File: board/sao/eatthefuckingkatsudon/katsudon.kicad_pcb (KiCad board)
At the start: 2 copper layers, 48.9 x 49.8 mm, 4 parts

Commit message: work on punching popuko sao
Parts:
- removed the G*** at (90.6, 73.6) (x4)
- added G*** (x4): LOGO, LOGO, F.Cu at (50.3, 41.6)
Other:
- board size 48.9 x 49.8 mm -> 48.2 x 48.9 mm

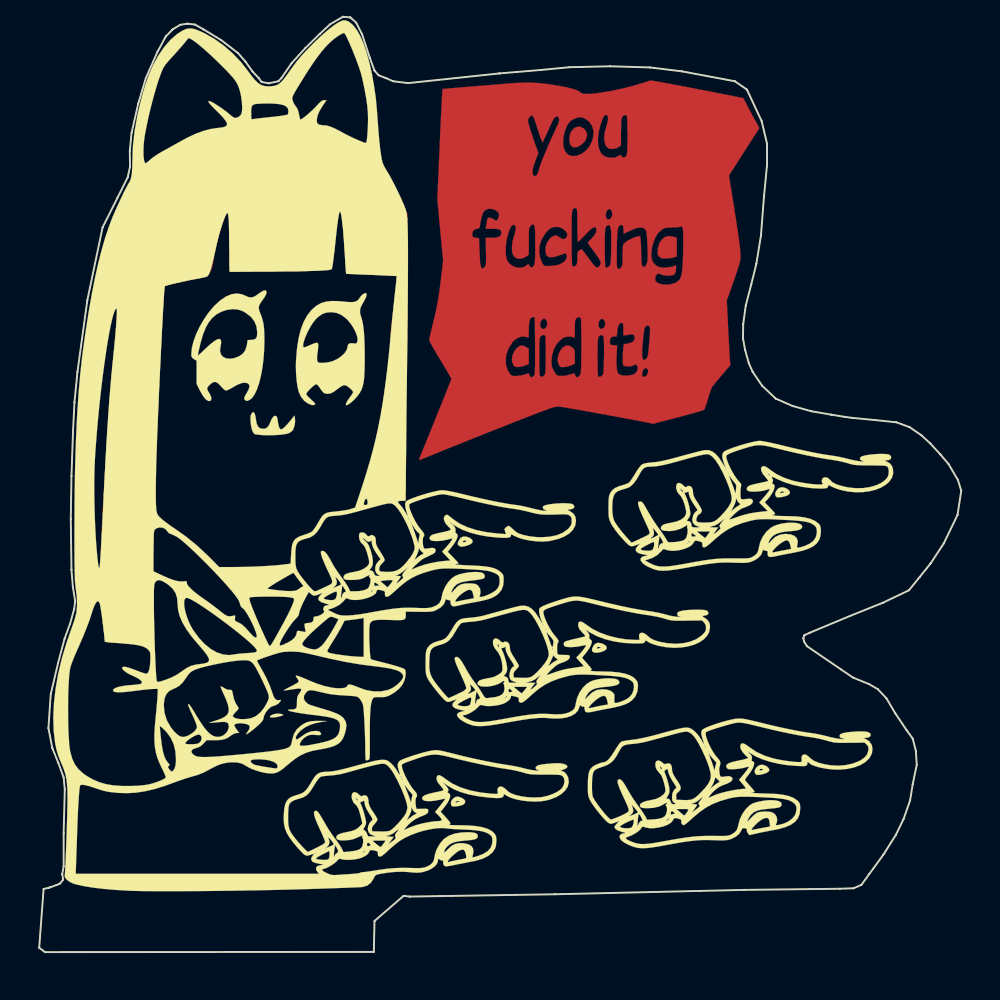
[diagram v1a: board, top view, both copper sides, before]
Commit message: wired power and LED matrix
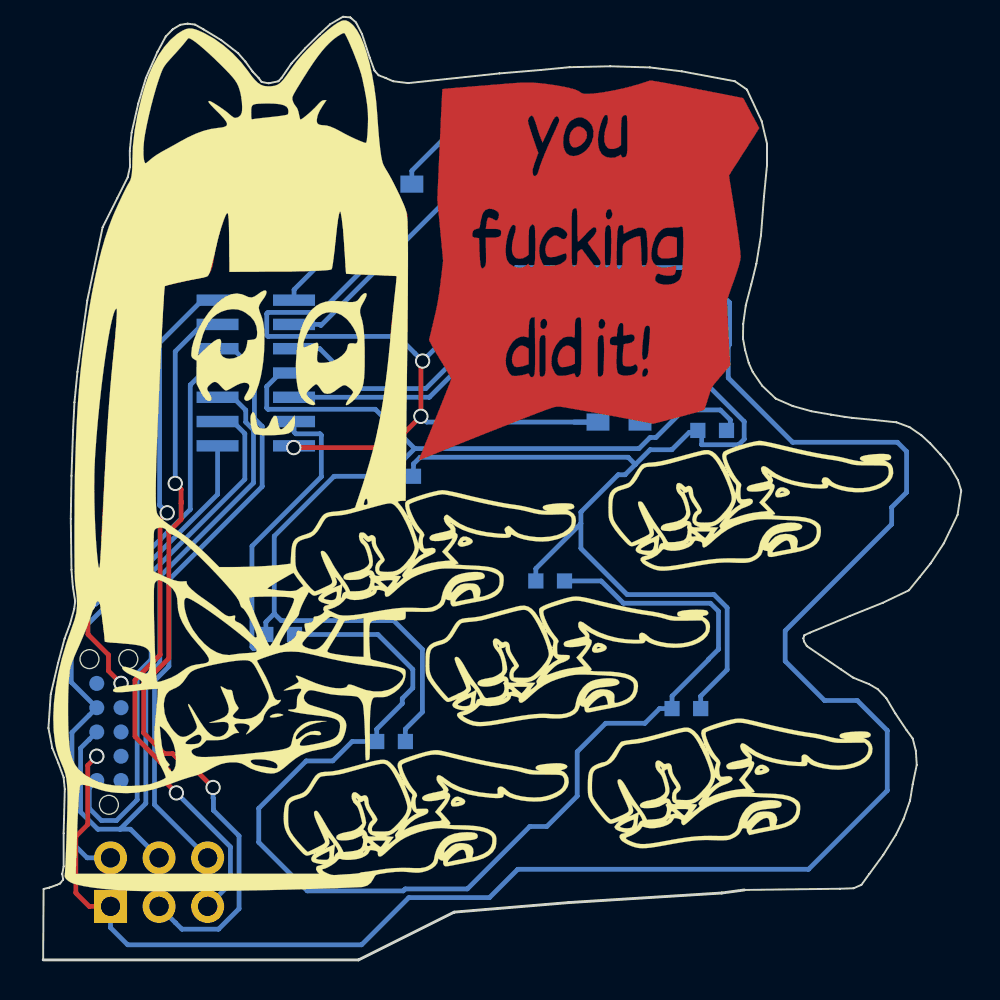
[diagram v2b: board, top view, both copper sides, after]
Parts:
- removed the G*** at (50.3, 41.6) (x4)
- added D1: LED, LEDs:LED_0603, B.Cu at (59.1, 53.9)
- added D2: LED, LEDs:LED_0603, B.Cu at (52.0, 47.2)
- added D3: LED, LEDs:LED_0603, B.Cu at (43.7, 55.6)
- added D4: LED, LEDs:LED_0603, B.Cu at (37.9, 50.0)
- added D5: LED, LEDs:LED_0603, B.Cu at (60.5, 39.3)
- added D6: LED, LEDs:LED_0603, B.Cu at (44.1, 41.7)
- added D7: LED, LEDs:LED_0603, B.Cu at (37.2, 24.4)
- added D8: LED, LEDs:LED_0603, B.Cu at (47.8, 23.9)
- added D9: LED, LEDs:LED_0603, B.Cu at (59.7, 34.8)
- added G*** (x4): LOGO, LOGO, F.Cu at (50.3, 41.6)
- added G***: LOGO, katsudon:GRANTSIG10X10, B.Cu at (45.2, 32.7)
- added IC1: ATTINY20-X, katsudon:ATTINY20_SOIC-14, B.Cu at (36.6, 36.3)
- added J1: PROG, katsudon:TC2050-All_Holes, B.Cu at (28.9, 55.1)
- added P1: SAO_PLUG, Socket_Strips:Socket_Strip_Straight_2x03, B.Cu at (29.0, 64.2)
- added R1: R, Resistors_SMD:R_0603_HandSoldering, B.Cu at (37.3, 26.5)
- added R2: R, Resistors_SMD:R_0603_HandSoldering, B.Cu at (43.7, 26.4)
- added R3: R, Resistors_SMD:R_0603_HandSoldering, B.Cu at (55.6, 38.9)
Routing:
- net GND: track 0.00 -> 171.0 mm, vias 0 -> 4
- net Net-(D1-Pad2): track 0.00 -> 81.3 mm
- net Net-(D1-Pad1): track 0.00 -> 74.1 mm
- net Net-(D3-Pad1): track 0.00 -> 58.0 mm
- net /SCL: track 0.00 -> 40.7 mm, vias 0 -> 2
- net /GPIO2: track 0.00 -> 36.9 mm, vias 0 -> 2
- net /SDA/TPIDATA: track 0.00 -> 36.4 mm
- net /GPIO1: track 0.00 -> 31.6 mm
- net /TPICLK: track 0.00 -> 28.0 mm
- net +3V3: track 0.00 -> 27.4 mm
- net Net-(D9-Pad2): track 0.00 -> 25.2 mm
- net /RESET: track 0.00 -> 20.5 mm, vias 0 -> 2
- net Net-(D8-Pad2): track 0.00 -> 13.8 mm
- net Net-(D7-Pad2): track 0.00 -> 9.96 mm
- net Net-(D8-Pad1): track 0.00 -> 5.18 mm
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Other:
- board size 48.2 x 48.9 mm -> 48 x 49.3 mm
- net class Default: clearance 0.2 -> 0.2032; via_dia 0.6 -> 0.8; via_drill 0.4 -> 0.6
- rule trace_clearance: 0.2 -> 0.2032
- rule trace_min: 0.2 -> 0.2032
- rule via_min_size: 0.4 -> 0.6
- board text added: "JLCJLCJLCJLC"
- board text added: "fuck you takeshobo!"
